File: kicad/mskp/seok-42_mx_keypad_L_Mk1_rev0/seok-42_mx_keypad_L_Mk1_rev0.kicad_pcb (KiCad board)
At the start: 2 copper layers, 162 x 117 mm, 44 parts, among them J1 Conn_01x12_Socket, SW1 Switch, SW10 Switch, SW11 Switch, SW12 Switch, SW13 Switch, SW14 Switch, SW15 Switch, SW16 Switch, SW17 Switch, SW18 Switch, SW19 Switch, SW2 Switch, SW20 Switch, SW21 Switch, SW3 Switch, SW4 Switch, SW5 Switch, SW6 Switch, SW7 Switch, SW8 Switch, SW9 Switch

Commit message: Continues work with rough PCB outlines
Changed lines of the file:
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@@
 		)
+	)
+	(gr_rect
+		(start 57 25)
+		(end 239 162)
+		(stroke
+			(width 0.2)
+			(type default)
+		)
+		(fill none)
+		(layer "F.Cu")
 	)
 	(gr_arc
@@
 		)
 		(layer "Edge.Cuts")
+	)
+	(dimension
+		(type aligned)
+		(layer "F.Cu")
+		(pts
+			(xy 218 152) (xy 218 162)
+		)
+		(height -6.75)
+		(gr_text "10.0000 mm"
+			(at 222.95 157 90)
+			(layer "F.Cu")
+			(effects
+				(font
+					(size 1.5 1.5)
+					(thickness 0.3)
+				)
+			)
+		)
+		(format
+			(prefix "")
+			(suffix "")
+			(units 3)
+			(units_format 1)
+			(precision 4)
+		)
+		(style
+			(thickness 0.2)
+			(arrow_length 1.27)
+			(text_position_mode 0)
+			(extension_height 0.58642)
+			(extension_offset 0.5) keep_text_aligned)
 	)
 	(dimension
@@
 			(layer "F.Cu")
 			(effects
+				(font
+					(size 1.5 1.5)
+					(thickness 0.3)
+				)
+			)
+		)
+		(format
+			(prefix "")
+			(suffix "")
+			(units 3)
+			(units_format 1)
+			(precision 4)
+		)
+		(style
+			(thickness 0.2)
+			(arrow_length 1.27)
+			(text_position_mode 0)
+			(extension_height 0.58642)
+			(extension_offset 0.5) keep_text_aligned)
+	)
+	(dimension
+		(type aligned)
+		(layer "F.Cu")
+		(pts
+			(xy 138 35) (xy 138 25)
+		)
+		(height 5.5)
+		(gr_text "10.0000 mm"
+			(at 141.7 30 90)
+			(layer "F.Cu")
+			(effects

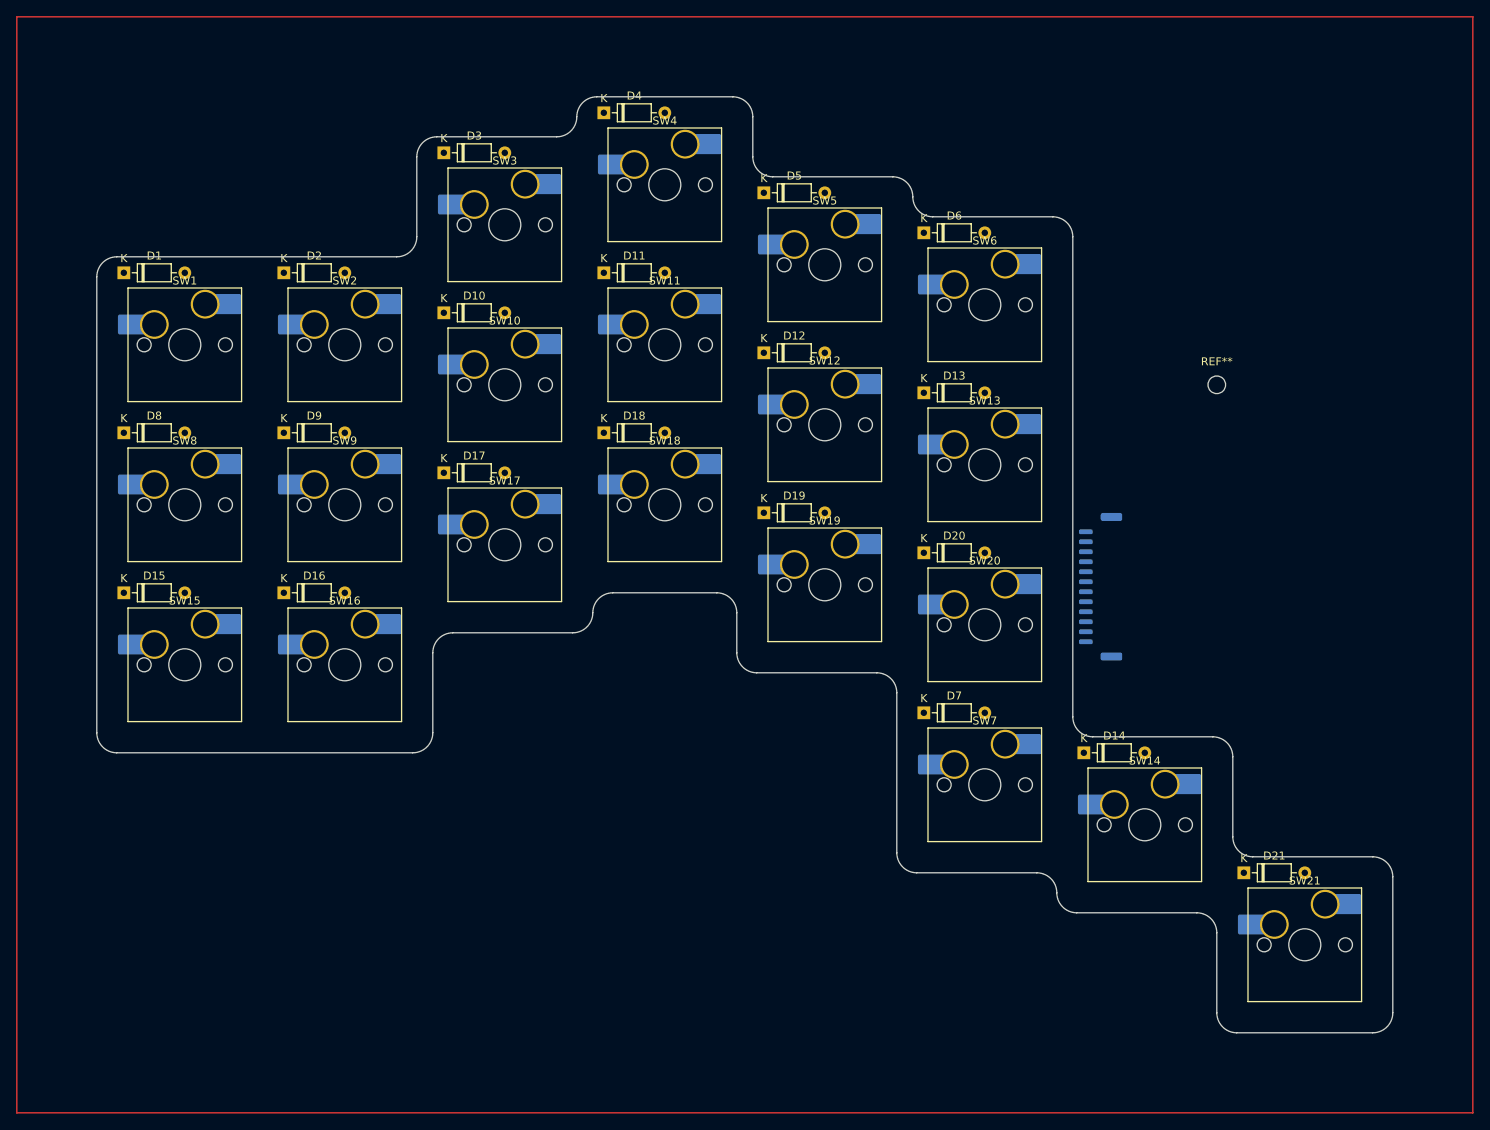
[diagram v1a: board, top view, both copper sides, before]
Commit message: Adds initial PCB layout for seok-42_mx_keypad_Mk1_rev0
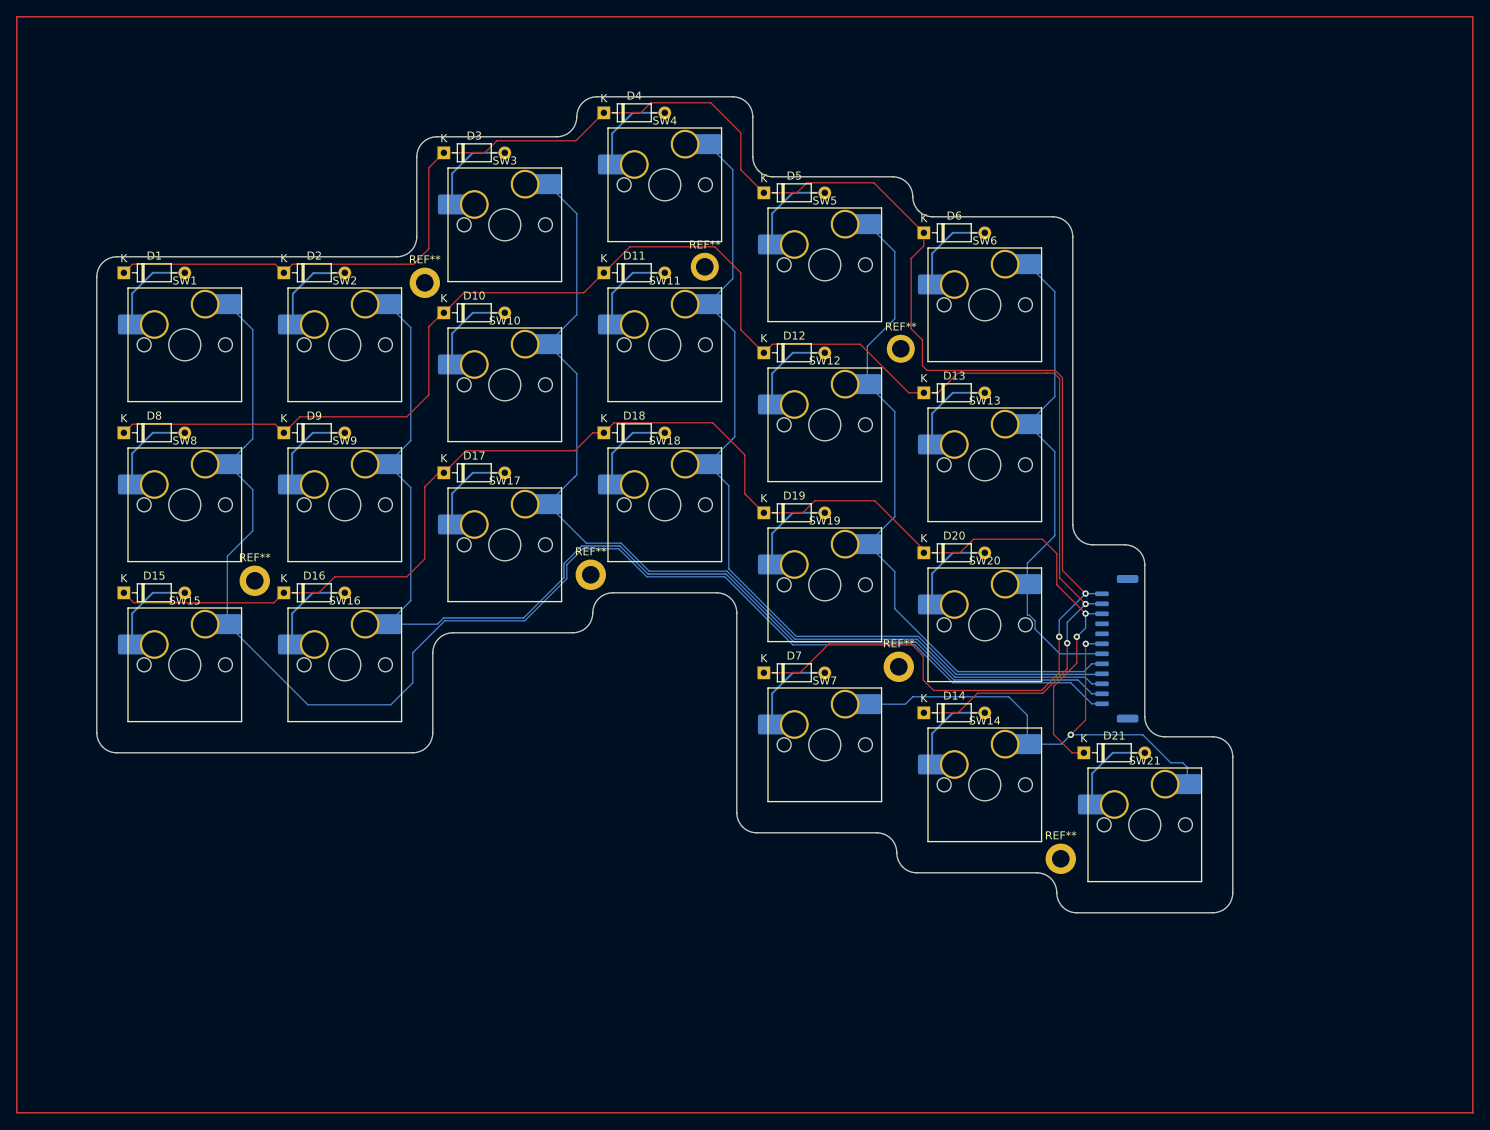
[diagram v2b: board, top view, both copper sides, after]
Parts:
- removed the REF** at (207.0, 71.0)
- added REF**: MountingHole_2.2mm_M2_ISO7380_Pad, MountingHole:MountingHole_2.2mm_M2_ISO7380_Pad, F.Cu at (143.0, 56.2)
- added REF**: MountingHole_2.2mm_M2_ISO7380_Pad, MountingHole:MountingHole_2.2mm_M2_ISO7380_Pad, F.Cu at (167.5, 66.5)
- added REF**: MountingHole_2.2mm_M2_ISO14580_Pad, MountingHole:MountingHole_2.2mm_M2_ISO14580_Pad, F.Cu at (86.8, 95.5)
- added REF**: MountingHole_2.2mm_M2_ISO14580_Pad, MountingHole:MountingHole_2.2mm_M2_ISO14580_Pad, F.Cu at (187.5, 130.2)
- added REF**: MountingHole_2.2mm_M2_ISO14580_Pad, MountingHole:MountingHole_2.2mm_M2_ISO14580_Pad, F.Cu at (108.0, 58.2)
- added REF**: MountingHole_2.2mm_M2_ISO14580_Pad, MountingHole:MountingHole_2.2mm_M2_ISO14580_Pad, F.Cu at (167.2, 106.2)
- added REF**: MountingHole_2.2mm_M2_ISO14580_Pad, MountingHole:MountingHole_2.2mm_M2_ISO14580_Pad, F.Cu at (128.8, 94.8)
- moved D21 25.0 mm to (190.4, 117.0)
- moved SW21 25.0 mm to (198.0, 126.0)
- moved D14 20.6 mm to (170.4, 112.0)
- moved D7 20.6 mm to (150.4, 107.0)
- moved SW14 20.6 mm to (178.0, 121.0)
- moved SW7 20.6 mm to (158.0, 116.0)
- moved J1 8.01 mm to (194.5, 104.0)
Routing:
- net Net-(D1-K): track 0.00 -> 247.1 mm, vias 0 -> 2
- net Net-(D10-K): track 0.00 -> 207.2 mm, vias 0 -> 2
- net Net-(J1-Pin_12): track 0.00 -> 178.1 mm
- net Net-(D15-K): track 0.00 -> 176.8 mm, vias 0 -> 2
- net Net-(J1-Pin_11): track 0.00 -> 146.9 mm
- net Net-(J1-Pin_10): track 0.00 -> 124.7 mm
- net Net-(J1-Pin_9): track 0.00 -> 113.5 mm
- net Net-(J1-Pin_8): track 0.00 -> 84.7 mm
- net Net-(J1-Pin_6): track 0.00 -> 63.4 mm, vias 0 -> 2
- net Net-(J1-Pin_7): track 0.00 -> 61.5 mm
- net Net-(D6-A): track 0.00 -> 11.5 mm
- net Net-(D5-A): track 0.00 -> 11.5 mm
- net Net-(D4-A): track 0.00 -> 11.5 mm
- net Net-(D11-A): track 0.00 -> 11.5 mm
- net Net-(D7-A): track 0.00 -> 11.5 mm
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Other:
- board size 162 x 117 mm -> 142 x 102 mm

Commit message: Adds silkscreen for seok-42_mx_keypad_L_Mk1_rev0 PCB
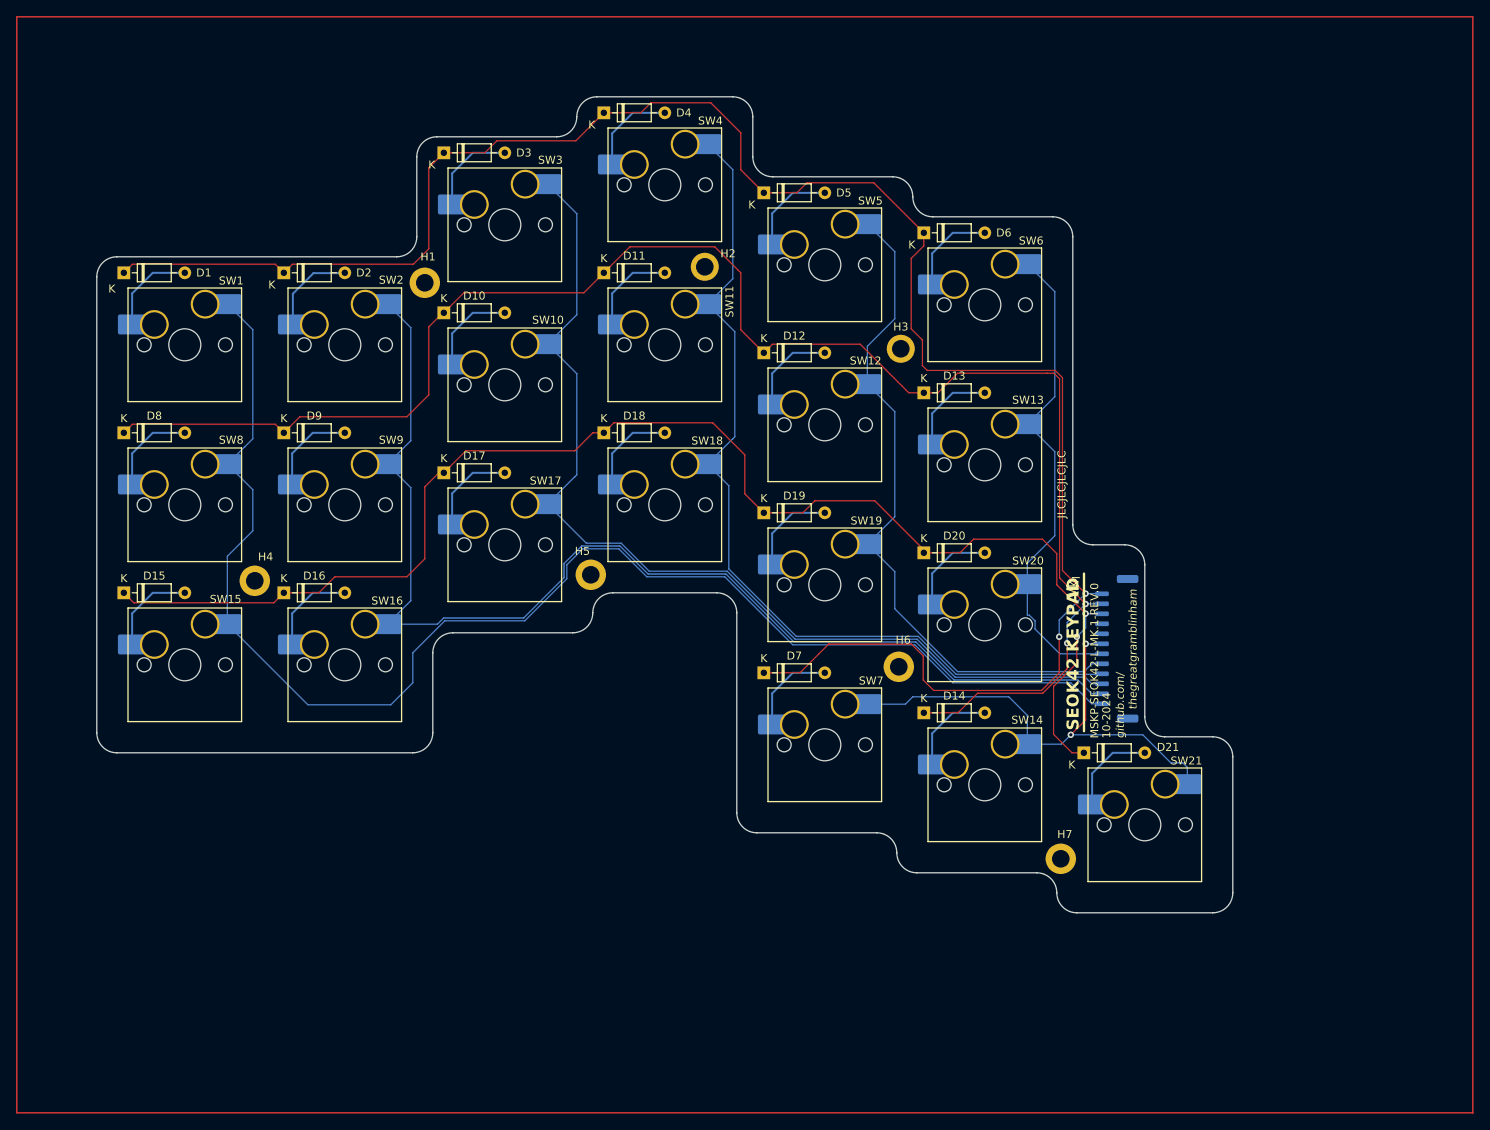
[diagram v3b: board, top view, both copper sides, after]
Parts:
- renumbered REF** to H1, REF** to H2, REF** to H3, REF** to H4, REF** to H5, REF** to H6, REF** to H7
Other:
- board text added: "10-2024"
- board text added: "CONTROL BOARD"
- board text added: "I"
- board text added: "JLCJLCJLCJLC"
- board text added: "MSKP-SEOK42-L-MK.1-REV.0"
- board text added: "Mk"
- board text added: "SEOK42 KEYPAD"
- board text added: "SW1"
- board text added: "SW10"
- board text added: "SW11"
- board text added: "SW12"
- board text added: "SW13"
- board text added: "SW14"
- board text added: "SW15"
- board text added: "SW16"
- board text added: "SW17"
- board text added: "SW18"
- board text added: "SW19"
- board text added: "SW2"
- board text added: "SW20"
- board text added: "SW21"
- board text added: "SW3"
- board text added: "SW4"
- board text added: "SW5"
- board text added: "SW6"
- board text added: "SW7"
- board text added: "SW8"
- board text added: "SW9"
- board text added: "github.com/"
- board text added: "thegreatgramblinham"
